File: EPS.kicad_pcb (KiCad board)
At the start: 4 copper layers, 90.2 x 95.9 mm, 91 parts, among them IC1 TPS22997RYZR, IC10 SN65HVD1782QDRQ1, IC11 MCP2518FDT-E_SL, IC12 MCP2518FDT-E_SL, IC2 TPS56C230RJER, IC3 TPS22997RYZR, IC7 TPS22997RYZR, IC8 TPS22997RYZR, IC9 TCAN1046AVDYYRQ1, J1 S4B-XH-A_LF__SN_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

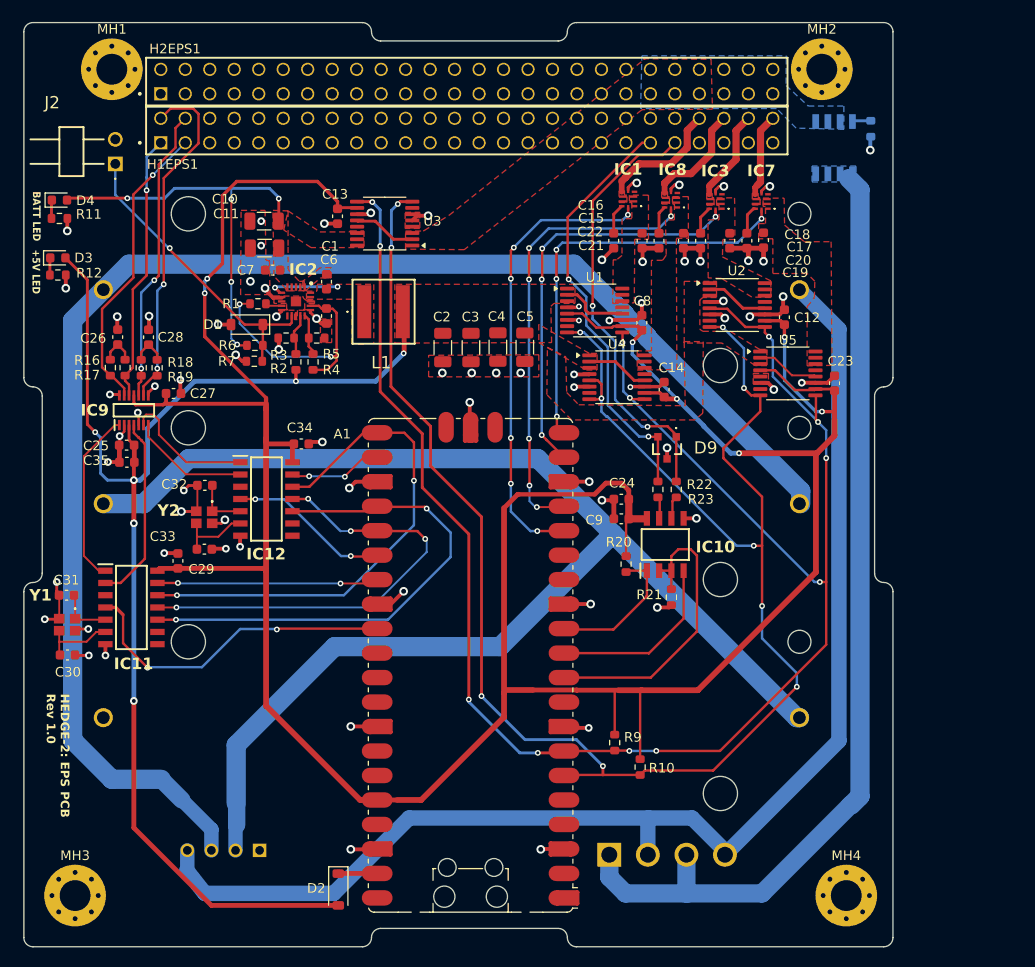
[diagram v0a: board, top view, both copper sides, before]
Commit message: updated schematic, began revising routing
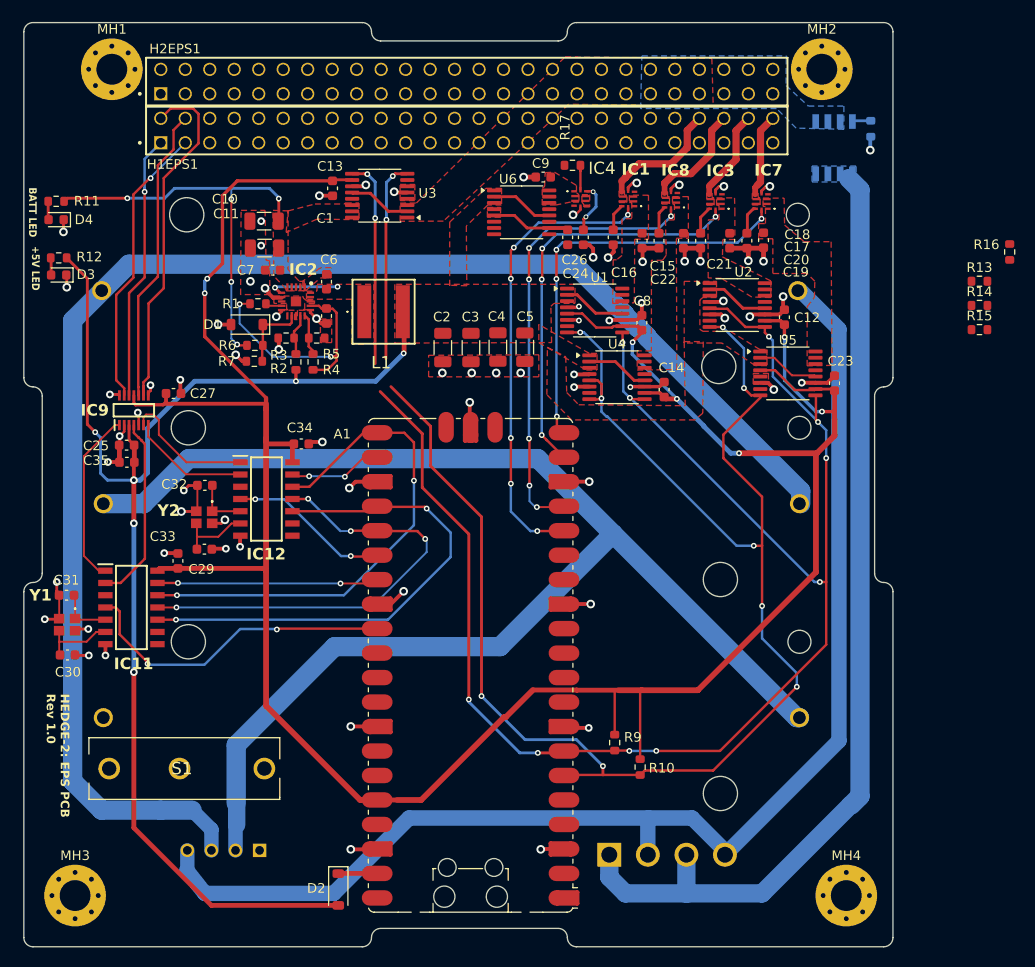
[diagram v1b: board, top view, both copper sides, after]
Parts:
- removed C28: 100n, Capacitor_SMD:C_0603_1608Metric
- removed D9: SM712-02HTG, HEDGE2-EPS:SM71202HTG
- removed IC10: SN65HVD1782QDRQ1, HEDGE2-EPS:SN65HVD1782QDRQ1
- removed J2: PH1RA-02-UA, HEDGE2-EPS:PH1RA02UA
- removed R18, R19: 60, Resistor_SMD:R_0603_1608Metric
- removed R20, R21: 10k, Resistor_SMD:R_0603_1608Metric
- removed R22, R23: 10, Resistor_SMD:R_0603_1608Metric
- added IC4: TPS22997RYZR, HEDGE2-EPS:TPS22997RYZR, F.Cu at (166.2, 71.3)
- added R13: 10k, Resistor_SMD:R_0603_1608Metric, F.Cu at (207.6, 79.9)
- added R14: 10k, Resistor_SMD:R_0603_1608Metric, F.Cu at (207.6, 82.4)
- added R15: 10k, Resistor_SMD:R_0603_1608Metric, F.Cu at (207.6, 84.9)
- added S1: SS-5D, HEDGE2-EPS:SS5D, F.Cu at (133.4, 130.5)
- added U6: INA260, Package_SO:TSSOP-16_4.4x5mm_P0.65mm, F.Cu at (160.1, 72.7)
- C24: value 100n -> 1n
- R11: value 4k7 -> 1k
- R12: value 2k2 -> 330
- R16, R17: value 60 -> 10k
- R8: value 10k -> 100k
- moved R16 94.1 mm to (210.8, 76.9)
- moved R17 50.9 mm to (165.4, 67.9), turned to 180 degrees
- moved C26 47.8 mm to (164.9, 75.3), turned to -90 degrees
- moved C9 36.4 mm to (162.4, 69.1)
- moved C24 27.5 mm to (166.5, 75.3), turned to -90 degrees
- moved C13 2.94 mm to (140.5, 70.3)
- moved U3 2.94 mm to (145.4, 71.0)
- moved D4 2.06 mm to (111.8, 73.5), turned to 180 degrees
- moved R11 1.81 mm to (111.8, 71.6), turned to 180 degrees
- moved D3 1.78 mm to (112.1, 79.2), turned to 180 degrees
- moved R12 1.78 mm to (112.1, 77.5), turned to 180 degrees
- moved C16 0.36 mm to (169.6, 75.3)
- moved BT3 0.19 mm to (152.7, 80.9)
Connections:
- net +5V_COMM renamed +5V_COMM_XBEE
- net +5V_COMM_SENSE renamed +5V_COMM_XBEE_SENSE
- net /EN renamed Net-(D1-K)
- A1 pad 10: /RS485_E -> unconnected-(A1-GPIO7-Pad10)
- A1 pad 11: /RS485_TX -> unconnected-(A1-GPIO8-Pad11)
- A1 pad 12: /RS485_RX -> unconnected-(A1-GPIO9-Pad12)
- A1 pad 16: /OBC_C -> unconnected-(A1-GPIO12-Pad16)
- A1 pad 17: /GNSS_C -> unconnected-(A1-GPIO13-Pad17)
- A1 pad 19: /SCI_C -> unconnected-(A1-GPIO14-Pad19)
- A1 pad 20: /COMM_C -> unconnected-(A1-GPIO15-Pad20)
- C24 pad 1: +3V3 -> Net-(IC4-CT)
- C26 pad 1: Net-(C26-Pad1) -> +3V3
- C9 pad 1: +3V3 -> +5V_COMM_DMR_SENSE
- D3 pad 1: Net-(D3-K) -> GND
- D3 pad 2: +5V -> Net-(D3-A)
- D4 pad 1: Net-(D4-K) -> GND
- D4 pad 2: +BATT_SENSE -> Net-(D4-A)
- H1EPS1 pad 41: /UART_G_TX (EPS) -> unconnected-(H1EPS1-Pad41)
- H1EPS1 pad 43: /UART_G_RX (EPS) -> unconnected-(H1EPS1-Pad43)
- H1EPS1 pad 51: unconnected-(H1EPS1-Pad51) -> +5V_COMM_DMR
- H2EPS1 pad 03: /RTS/DIO6_XB -> unconnected-(H2EPS1-Pad03)
- H2EPS1 pad 04: /CTS/DIO7_XB -> unconnected-(H2EPS1-Pad04)
- H2EPS1 pad 05: /AD3/DIO3/SPI_SSEL_XB -> unconnected-(H2EPS1-Pad05)
- H2EPS1 pad 06: /AD/DIO2/SPI_CLK_XB -> unconnected-(H2EPS1-Pad06)
- H2EPS1 pad 07: /DIO4/SPI_MOSI_XB -> unconnected-(H2EPS1-Pad07)
- H2EPS1 pad 08: /DIO12/SPI_MISO_XB -> unconnected-(H2EPS1-Pad08)
- H2EPS1 pad 10: /AD1/DIO1/SPI_ATTN_XB -> unconnected-(H2EPS1-Pad10)
- H2EPS1 pad 12: /DIO10/PWM0_XB -> unconnected-(H2EPS1-Pad12)
- H2EPS1 pad 14: /DIO11/PWM1_XB -> unconnected-(H2EPS1-Pad14)
- H2EPS1 pad 15: /AD0/DIO0_XB -> unconnected-(H2EPS1-Pad15)
- H2EPS1 pad 17: /NDTR_XB -> unconnected-(H2EPS1-Pad17)
- H2EPS1 pad 23: /SPKEN_DMR -> unconnected-(H2EPS1-Pad23)
- H2EPS1 pad 24: /CS_DMR -> unconnected-(H2EPS1-Pad24)
- H2EPS1 pad 25: /HST_RXD_DMR -> unconnected-(H2EPS1-Pad25)
- H2EPS1 pad 27: /HST_TXD_DMR -> unconnected-(H2EPS1-Pad27)
- IC1 pad 10: /OBC_C -> Net-(IC1-ON)
- IC3 pad 10: /SCI_C -> Net-(IC3-ON)
- IC7 pad 10: /COMM_C -> Net-(IC7-ON)
- IC8 pad 10: /GNSS_C -> Net-(IC8-ON)
- R11 pad 1: Net-(D4-K) -> +BATT_SENSE
- R11 pad 2: GND -> Net-(D4-A)
- R12 pad 1: Net-(D3-K) -> +5V
- R12 pad 2: GND -> Net-(D3-A)
- R16 pad 1: /CAN_A_H -> Net-(IC7-ON)
- R16 pad 2: Net-(C26-Pad1) -> /COMM_XBEE_C
- R17 pad 1: Net-(C26-Pad1) -> Net-(IC4-ON)
- R17 pad 2: /CAN_A_L -> /COMM_DMR_C
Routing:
- net /UART_G_RX (EPS): track 45.4 -> 0.00 mm, vias 2 -> 0
- net /UART_G_TX (EPS): track 44.2 -> 0.00 mm, vias 2 -> 0
- net /COMM_C: track 42.9 -> 0.00 mm, vias 4 -> 0
- net (no net): track 0.00 -> 42.9 mm, vias 0 -> 4
- net +3V3: track 313.7 -> 276.4 mm
- net /RS485_E: track 31.6 -> 0.00 mm
- net Net-(D1-K): track 31.9 -> 7.67 mm, vias 1 -> 0
- net /RS485_TX: track 18.9 -> 0.00 mm
- net /RS485_RX: track 14.9 -> 0.00 mm
- net GND: track 137.1 -> 130.5 mm, vias 75 -> 72
- net +5V: track 162.5 -> 168.5 mm
- net Net-(IC4-CT): track 0.00 -> 5.45 mm, vias 0 -> 2
- net Net-(C28-Pad1): track 3.83 -> 0.00 mm
- net Net-(C26-Pad1): track 3.78 -> 0.00 mm
- net /VC2: track 153.1 -> 156.7 mm
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- added copper zone on F.Cu, net +3V3
- added copper zone on F.Cu, net +5V_COMM_DMR
- added copper zone on F.Cu, net +5V_COMM_DMR_SENSE

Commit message: implemented updates
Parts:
- D3, D4: footprint LED_SMD:LED_0603_1608Metric -> LED_THT:LED_D3.0mm
- R11: value 1k -> 820; footprint Resistor_SMD:R_0603_1608Metric -> Resistor_SMD:R_0805_2012Metric
- R12: footprint Resistor_SMD:R_0603_1608Metric -> Resistor_SMD:R_0805_2012Metric
- moved J1 48.9 mm to (181.9, 139.0)
- moved R13 48.8 mm to (158.9, 78.3), turned to -90 degrees
- moved R14 47.3 mm to (160.5, 78.3), turned to -90 degrees
- moved R16 47.1 mm to (163.7, 78.3), turned to -90 degrees
- moved R15 46.0 mm to (162.1, 78.3), turned to -90 degrees
- moved J4 44.0 mm to (125.3, 141.5)
- moved R17 13.3 mm to (157.1, 78.3), turned to -90 degrees
- moved D4 8.44 mm to (110.8, 65.1), turned to -90 degrees
- moved R12 3.88 mm to (111.7, 81.3)
- moved D2 3.31 mm to (141.4, 139.7), turned to 90 degrees
- moved D3 3.06 mm to (110.8, 76.5), turned to -90 degrees
- moved R11 1.50 mm to (111.8, 70.1)
- moved C24 0.97 mm to (167.2, 74.7), turned to 0 degrees
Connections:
- A1 pad 15: unconnected-(A1-GPIO11-Pad15) -> /OBC_C
- A1 pad 16: unconnected-(A1-GPIO12-Pad16) -> /GNSS_C
- A1 pad 17: unconnected-(A1-GPIO13-Pad17) -> /SCI_C
- A1 pad 19: unconnected-(A1-GPIO14-Pad19) -> /COMM_XBEE_C
- A1 pad 20: unconnected-(A1-GPIO15-Pad20) -> /COMM_DMR_C
- BT3 pad P: +BATT_BSW -> +BATT_BIN
- C15 pad 1: +5V_OBC_SENSE -> +5V_GNSS_SENSE
- C17 pad 1: +5V_SCI_SENSE -> +5V_COMM_XBEE_SENSE
- C19 pad 1: +5V_COMM_XBEE_SENSE -> +5V_COMM_DMR_SENSE
- C21 pad 1: +5V_GNSS_SENSE -> +5V_SCI_SENSE
- C9 pad 1: +5V_COMM_DMR_SENSE -> +5V_OBC_SENSE
- IC1 pad 1: +5V_OBC_SENSE -> +5V_GNSS_SENSE
- IC1 pad 2: +5V_OBC_SENSE -> +5V_GNSS_SENSE
- IC1 pad 3: +5V_OBC_SENSE -> +5V_GNSS_SENSE
- IC1 pad 6: +5V_OBC -> +5V_GNSS
- IC1 pad 7: +5V_OBC -> +5V_GNSS
- IC1 pad 8: +5V_OBC -> +5V_GNSS
- IC3 pad 1: +5V_SCI_SENSE -> +5V_COMM_XBEE_SENSE
- IC3 pad 2: +5V_SCI_SENSE -> +5V_COMM_XBEE_SENSE
- IC3 pad 3: +5V_SCI_SENSE -> +5V_COMM_XBEE_SENSE
- IC3 pad 6: +5V_SCI -> +5V_COMM_XBEE
- IC3 pad 7: +5V_SCI -> +5V_COMM_XBEE
- IC3 pad 8: +5V_SCI -> +5V_COMM_XBEE
- IC4 pad 1: +5V_COMM_DMR_SENSE -> +5V_OBC_SENSE
- IC4 pad 2: +5V_COMM_DMR_SENSE -> +5V_OBC_SENSE
- IC4 pad 3: +5V_COMM_DMR_SENSE -> +5V_OBC_SENSE
- IC4 pad 6: +5V_COMM_DMR -> +5V_OBC
- IC4 pad 7: +5V_COMM_DMR -> +5V_OBC
- IC4 pad 8: +5V_COMM_DMR -> +5V_OBC
- IC7 pad 1: +5V_COMM_XBEE_SENSE -> +5V_COMM_DMR_SENSE
- IC7 pad 2: +5V_COMM_XBEE_SENSE -> +5V_COMM_DMR_SENSE
- IC7 pad 3: +5V_COMM_XBEE_SENSE -> +5V_COMM_DMR_SENSE
- IC7 pad 6: +5V_COMM_XBEE -> +5V_COMM_DMR
- IC7 pad 7: +5V_COMM_XBEE -> +5V_COMM_DMR
- IC7 pad 8: +5V_COMM_XBEE -> +5V_COMM_DMR
- IC8 pad 1: +5V_GNSS_SENSE -> +5V_SCI_SENSE
- IC8 pad 2: +5V_GNSS_SENSE -> +5V_SCI_SENSE
- IC8 pad 3: +5V_GNSS_SENSE -> +5V_SCI_SENSE
- IC8 pad 6: +5V_GNSS -> +5V_SCI
- IC8 pad 7: +5V_GNSS -> +5V_SCI
- IC8 pad 8: +5V_GNSS -> +5V_SCI
- J1 pad 4: +BATT_BSW -> +BATT_BIN
- J4 pad A2: +BATT_BSW -> +BATT_AIN
- J4 pad A4: +BATT_BSW -> +BATT_AIN
- R13 pad 2: /OBC_C -> /GNSS_C
- R14 pad 2: /GNSS_C -> /SCI_C
- R15 pad 2: /SCI_C -> /COMM_XBEE_C
- R16 pad 2: /COMM_XBEE_C -> /COMM_DMR_C
- R17 pad 2: /COMM_DMR_C -> /OBC_C
- S1 pad 1: unconnected-(S1-COM-Pad1) -> +BATT_BIN
- S1 pad 3: unconnected-(S1-NC-Pad3) -> +BATT_AIN
- U1 pad 14: +5V_OBC_SENSE -> +5V_GNSS_SENSE
- U1 pad 15: +5V_OBC_SENSE -> +5V_GNSS_SENSE
- U1 pad 16: +5V_OBC_SENSE -> +5V_GNSS_SENSE
- U2 pad 14: +5V_SCI_SENSE -> +5V_COMM_XBEE_SENSE
- U2 pad 15: +5V_SCI_SENSE -> +5V_COMM_XBEE_SENSE
- U2 pad 16: +5V_SCI_SENSE -> +5V_COMM_XBEE_SENSE
- U4 pad 14: +5V_GNSS_SENSE -> +5V_SCI_SENSE
- U4 pad 15: +5V_GNSS_SENSE -> +5V_SCI_SENSE
- U4 pad 16: +5V_GNSS_SENSE -> +5V_SCI_SENSE
- U5 pad 14: +5V_COMM_XBEE_SENSE -> +5V_COMM_DMR_SENSE
- U5 pad 15: +5V_COMM_XBEE_SENSE -> +5V_COMM_DMR_SENSE
- U5 pad 16: +5V_COMM_XBEE_SENSE -> +5V_COMM_DMR_SENSE
- U6 pad 14: +5V_COMM_DMR_SENSE -> +5V_OBC_SENSE
- U6 pad 15: +5V_COMM_DMR_SENSE -> +5V_OBC_SENSE
- U6 pad 16: +5V_COMM_DMR_SENSE -> +5V_OBC_SENSE
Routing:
- net +BATT_BSW: track 133.2 -> 0.00 mm
- net +BATT_BIN: track 0.00 -> 121.8 mm
- net +BATT_ASW: track 101.8 -> 151.3 mm
- net (no net): track 42.9 -> 0.00 mm, vias 4 -> 0
- net /VC1: track 144.4 -> 102.7 mm
- net /VC2: track 156.7 -> 197.9 mm
- net +BATT_AIN: track 0.00 -> 30.4 mm
- net Net-(IC7-ON): track 0.00 -> 24.4 mm, vias 0 -> 2
- net /SCL: track 183.6 -> 205.2 mm, vias 12 -> 14
- net Net-(IC3-ON): track 0.00 -> 21.1 mm, vias 0 -> 2
- net /COMM_XBEE_C: track 0.00 -> 20.0 mm, vias 0 -> 2
- net Net-(IC8-ON): track 0.00 -> 18.1 mm, vias 0 -> 2
- net /COMM_DMR_C: track 0.00 -> 16.8 mm, vias 0 -> 2
- net /GNSS_C: track 47.0 -> 30.9 mm, vias 6 -> 2
- net Net-(IC1-ON): track 0.00 -> 15.3 mm, vias 0 -> 2
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- added copper zone on B.Cu, net GND
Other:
- rule pad_to_mask_clearance: 0 -> 0.0508
